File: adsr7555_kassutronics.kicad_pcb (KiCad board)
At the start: 2 copper layers, 81.3 x 104.1 mm, 49 parts, among them J1 Power, J2 GateIn, J3 Trigger, J4 Gate, J5 Atten Out, J6 Output, Q1 NPN, Q2 NPN, Q3 NPN, Q4 NPN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

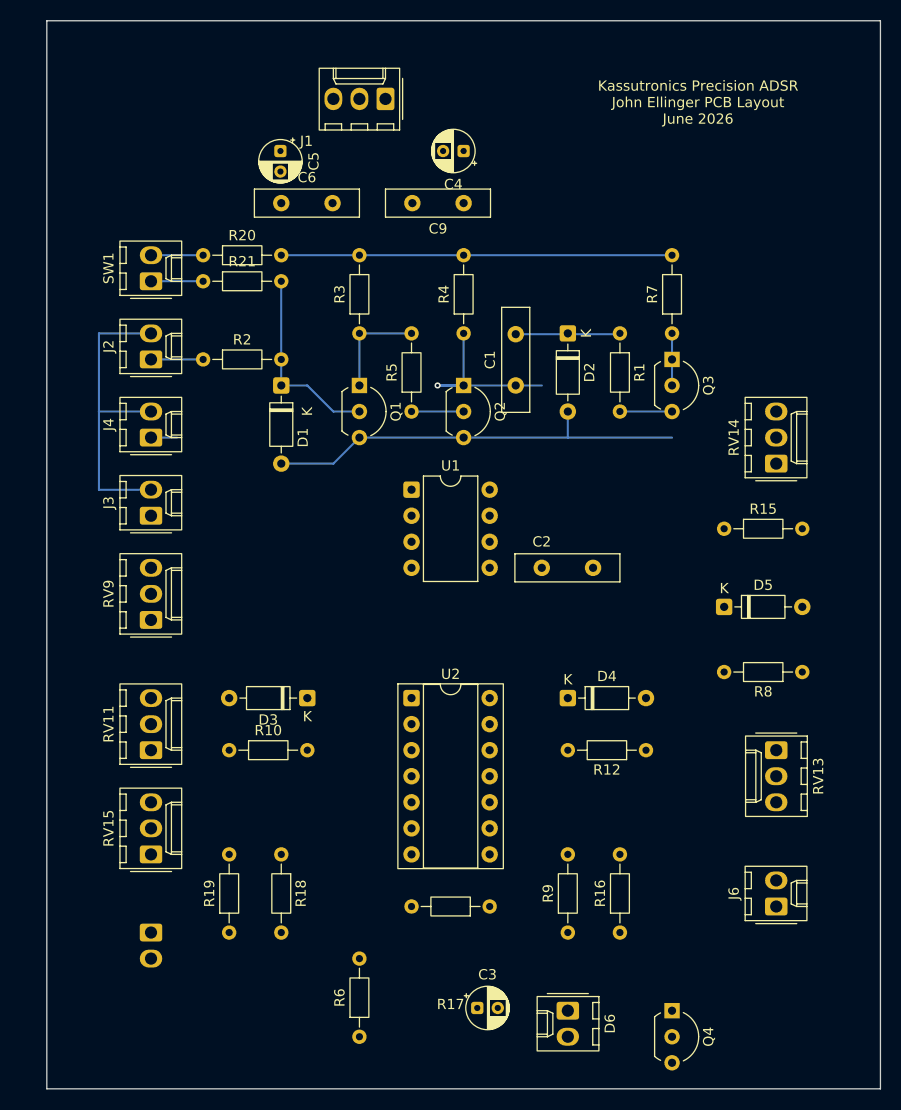
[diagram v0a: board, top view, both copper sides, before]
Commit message: PCB Wiring complete. Need to fix silkscreen overlaps
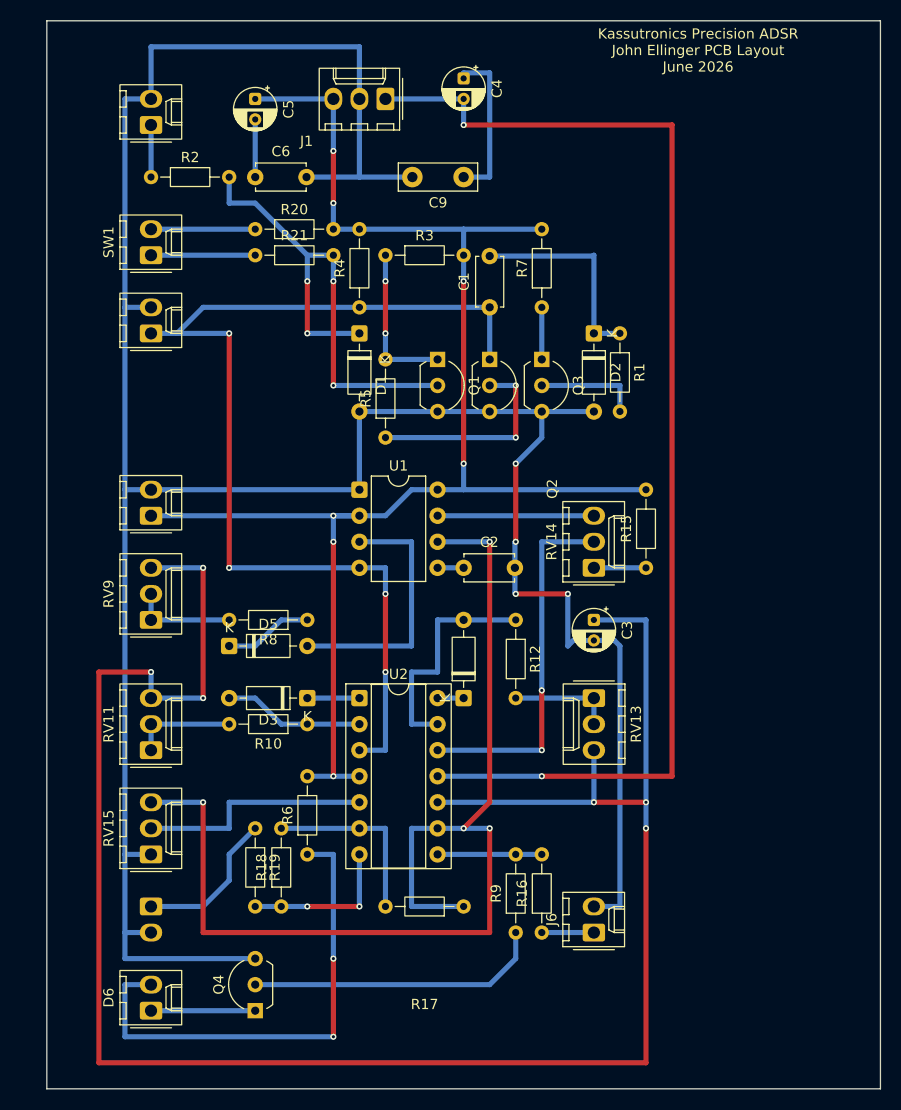
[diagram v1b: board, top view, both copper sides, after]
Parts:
- C1, C2, C6: footprint Capacitor_THT:C_Disc_D10.0mm_W2.5mm_P5.00mm -> Capacitor_THT:C_Disc_D4.7mm_W2.5mm_P5.00mm
- C9: footprint Capacitor_THT:C_Disc_D10.0mm_W2.5mm_P5.00mm -> Capacitor_THT:C_Disc_D7.5mm_W2.5mm_P5.00mm
- moved R8 48.5 mm to (50.8, 83.8)
- moved D5 48.4 mm to (43.2, 86.4)
- moved D6 40.6 mm to (35.6, 121.9), turned to 90 degrees
- moved Q4 40.6 mm to (45.7, 121.9), turned to 90 degrees
- moved C3 39.5 mm to (78.7, 83.8), turned to -90 degrees
- moved J2 22.9 mm to (35.6, 35.6)
- moved RV14 20.5 mm to (78.7, 78.7)
- moved R2 18.5 mm to (35.6, 40.6)
- moved RV13 18.5 mm to (78.7, 91.4)
- moved R6 18.5 mm to (50.8, 106.7)
- moved J6 18.0 mm to (78.7, 114.3)
- moved R12 18.0 mm to (71.1, 83.8), turned to -90 degrees
- moved R7 13.0 mm to (73.7, 53.3)
- moved Q3 12.7 mm to (73.7, 58.4)
- moved R4 10.5 mm to (55.9, 53.3)
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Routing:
- net GND: track 72.2 -> 271.0 mm, vias 0 -> 4
- net Net-(U2C-+): track 0.00 -> 195.6 mm, vias 0 -> 6
- net -15V: track 0.00 -> 116.8 mm, vias 0 -> 2
- net Net-(U1-THRES): track 0.00 -> 110.3 mm, vias 0 -> 4
- net +15V: track 38.1 -> 148.4 mm, vias 0 -> 7
- net /GATE: track 20.3 -> 102.7 mm, vias 1 -> 4
- net Net-(D6-A): track 0.00 -> 48.3 mm, vias 0 -> 2
- net Net-(U2D-+): track 0.00 -> 35.6 mm, vias 0 -> 2
- net Net-(D1-K): track 18.8 -> 50.4 mm, vias 0 -> 4
- net Net-(Q4-B): track 0.00 -> 29.0 mm
- net Net-(D5-A): track 0.00 -> 25.4 mm
- net Net-(D4-A): track 0.00 -> 22.9 mm
- net Net-(U2B-+): track 0.00 -> 22.9 mm
- net Net-(U2B--): track 0.00 -> 17.8 mm
- net Net-(C4-Pad1): track 0.00 -> 15.8 mm
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
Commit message: QA PCB passes
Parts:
- C4, C5: value C_Polarized_US -> 100u
- C9: footprint Capacitor_THT:C_Disc_D7.5mm_W2.5mm_P5.00mm -> Capacitor_THT:C_Disc_D4.7mm_W2.5mm_P5.00mm
- J5: value Atten Out -> Atn Out
- Q1, Q2, Q3, Q4: value NPN -> 3904
- RV11: value 1M Log Release -> 1M Log Rel
- RV13: value 1M Log Decay -> 1M Log Dky
- RV14: value 10K Lin Sustain -> 10K Lin Sus
- RV15: value 100k Lin Atten -> 100k Lin Atn; footprint Connector_Molex:Molex_KK-254_AE-6410-03A_1x03_P2.54mm_Vertical -> Potentiometer_THT:Potentiometer_Bourns_3296W_Vertical
- RV9: value 1M Log Attack -> 1M Log Atk
- U1: value ICM7555xP -> 7555
- turned RV15 to -90 degrees
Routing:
- net GND: track 271.0 -> 270.3 mm
- net +15V: vias 7 -> 6
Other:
- board size 81.3 x 104.1 mm -> 68.6 x 104.1 mm

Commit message: removed TRIG and GATE panel connectors
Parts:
- removed J3: Trigger, Connector_Molex:Molex_KK-254_AE-6410-02A_1x02_P2.54mm_Vertical
- removed J4: Gate, Connector_Molex:Molex_KK-254_AE-6410-02A_1x02_P2.54mm_Vertical
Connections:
- Q3 pad 1: Net-(Q3-C) -> /TRIG
- R7 pad 1: Net-(Q3-C) -> /TRIG
- U1 pad 2: +15V -> /TRIG
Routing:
- net /TRIG: track 0.00 -> 43.2 mm, vias 0 -> 2
- net +15V: track 148.4 -> 125.5 mm, vias 6 -> 4
- net /GATE: track 102.7 -> 81.3 mm, vias 4 -> 2
- net Net-(D5-A): track 25.4 -> 15.2 mm, vias 0 -> 2
- net Net-(Q3-C): track 5.08 -> 0.00 mm
- net GND: track 270.3 -> 267.7 mm, vias 4 -> 8
